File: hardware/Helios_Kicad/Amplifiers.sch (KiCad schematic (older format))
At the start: 31 parts, among them U6 TL084_v, U7 LM358, U8 TL084_v

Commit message: redone pcb, driver and firmware working-ish
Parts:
- removed R22, R23: 10k, Resistors_SMD:R_0603, symbol R
- added R16, R17, R24, R25, R30, R41, R42: 5.11k, Resistors_SMD:R_0603, symbol R
- added R18, R19: 10k, Resistors_SMD:R_0603, symbol R
- added R33, R34: 1.65k, Resistors_SMD:R_0603, symbol R
- renumbered C12 to C13, C13 to C14, C14 to C15, C15 to C16, C16 to C17, C17 to C18, R18 to R14, R19 to R15, R24 to R22, R25 to R23, R30 to R31, R31 to R32, R32 to R35, R33 to R36, R34 to R37, R35 to R38, R36 to R39, R37 to R40, R38 to R43, R39 to R44
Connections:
- net -B is gone; now on net +B: U6.7 (Out)
- net -R is gone; now on net +R: U6.14 (Out)
- net +B: now also R21.1; no longer R21.2
- net +G: now also R29.1, U6.8 (Out); no longer R26.2
- net +Intensity: now also R28.1, U6.1 (Out); no longer R27.2
- net +R: now also R20.1; no longer R20.2
- net GND: now also R20.2, R21.2, R26.1, R27.1, R28.2, R29.2, R18.1, R19.1, R41.2, R42.2; no longer U6.10 (+In), U6.12 (+In), U6.3 (+In), U6.5 (+In), U8.12 (+In), U8.5 (+In)
- net Offset: now also R33.2, R34.2; no longer U8.10 (+In), U8.3 (+In)
- net Shutter: now also R30.2; no longer U7.5 (+)
- net at U6.13 (-In): now also R18.2; no longer R20.1
- net at U6.6 (-In): now also R19.2; no longer R21.1
- removed net -G: R28.1, U6.8 (Out)
- removed net -Intensity: R29.1, U6.1 (Out)
- new net: R33.1, U8.3 (+In)
- new net: R42.1, U8.5 (+In)
- new net: R41.1, U8.12 (+In)
- new net: R34.1, U8.10 (+In)
- new net: R16.1, U6.12 (+In)
- new net: R24.1, U6.10 (+In)
- new net: R27.2, U6.9 (-In)
- new net: R17.1, U6.5 (+In)
- new net: R26.2, U6.2 (-In)
- new net: R25.1, U6.3 (+In)
- new net: R30.1, U7.5 (+)
- new net B: R17.2
- new net G: R24.2
- new net Intensity: R25.2
- new net R: R16.2
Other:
- moved on the sheet: U6A, U6B

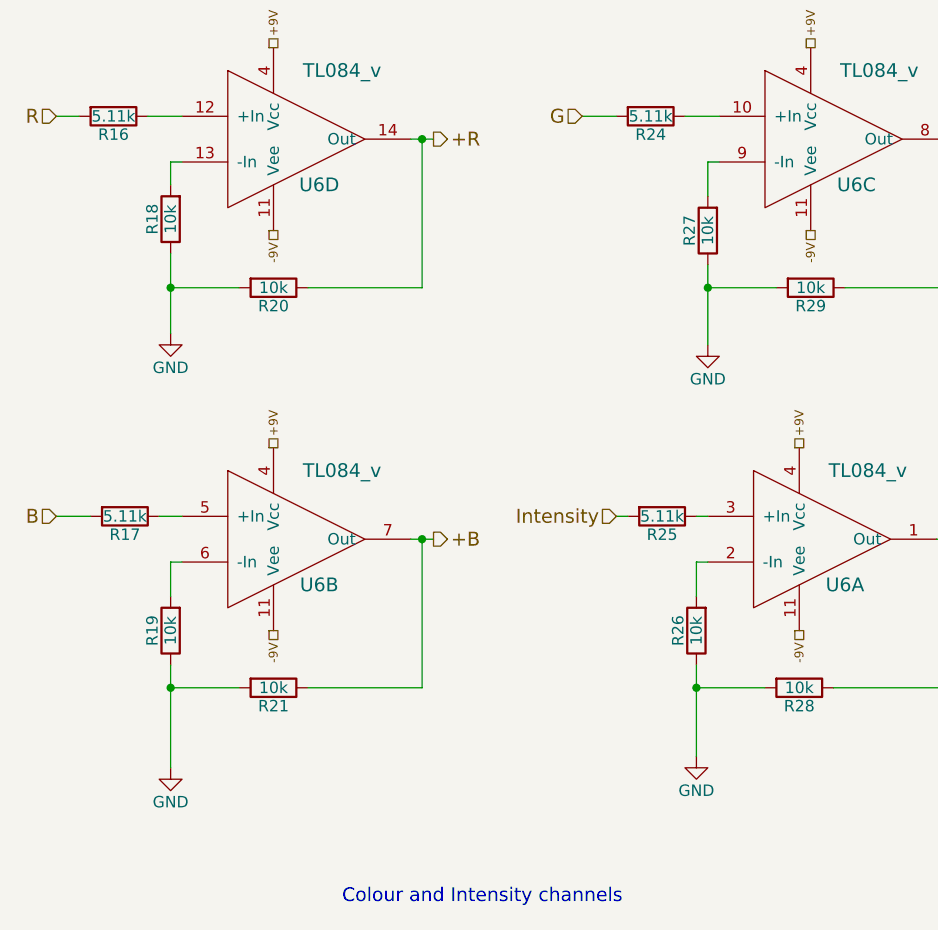
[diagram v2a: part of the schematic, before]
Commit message: fix color amps error
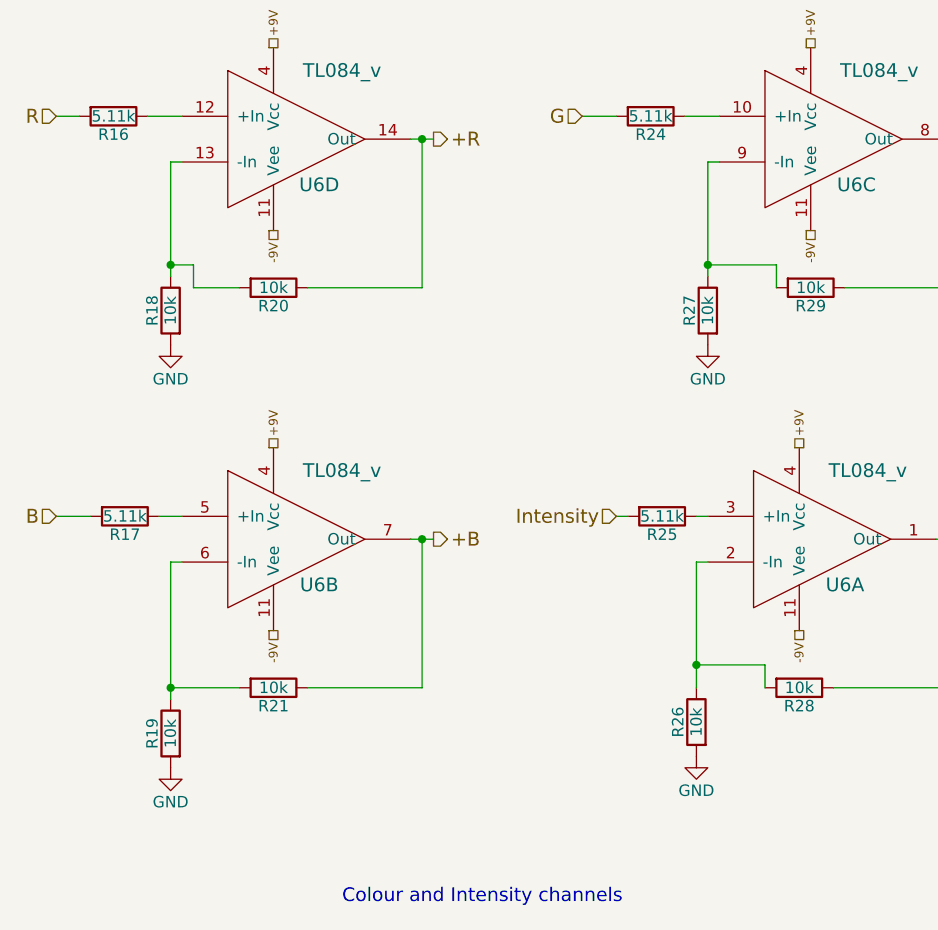
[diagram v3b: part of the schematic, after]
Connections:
- net GND: now also R18.2, R19.2, R26.2, R27.2; no longer R18.1, R19.1, R20.2, R21.2, R26.1, R27.1, R28.2, R29.2
- net at U6.13 (-In): now also R18.1, R20.2; no longer R18.2
- net at U6.9 (-In): now also R27.1, R29.2; no longer R27.2
- net at U6.6 (-In): now also R19.1, R21.2; no longer R19.2
- net at U6.2 (-In): now also R26.1, R28.2; no longer R26.2
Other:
- moved on the sheet: R18

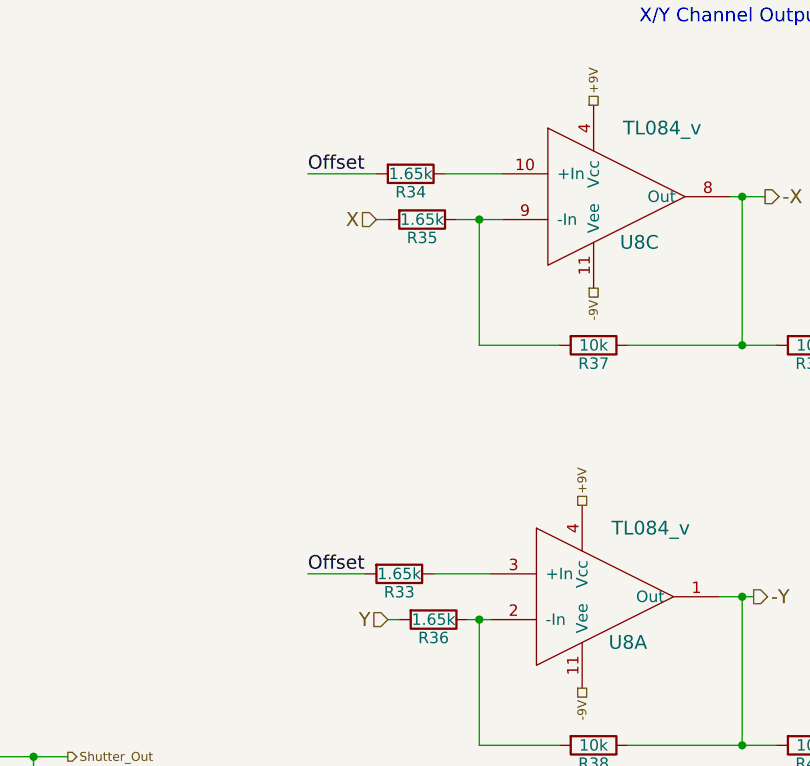
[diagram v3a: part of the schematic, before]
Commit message: removed uneccessary resistors
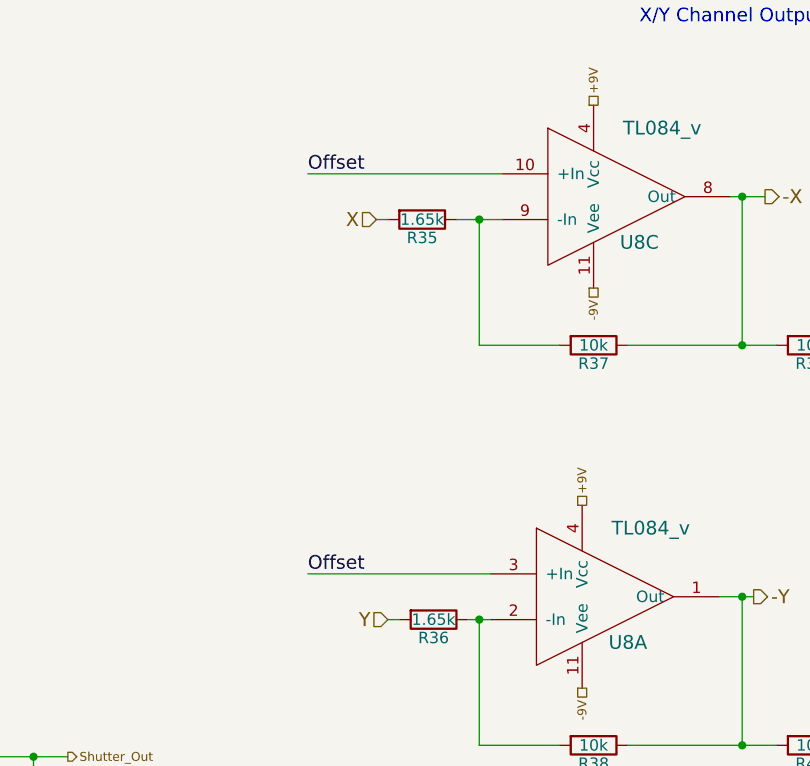
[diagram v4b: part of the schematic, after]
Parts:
- removed R33, R34: 1.65k, Resistors_SMD:R_0603, symbol R
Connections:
- net Offset: now also U8.10 (+In), U8.3 (+In)
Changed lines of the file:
@@
 	2800 6400 2800 6550
 Wire Wire Line
-	7650 3600 7900 3600
-Wire Wire Line
-	7600 5350 7850 5350
+	7050 3600 7900 3600
+Wire Wire Line
+	7050 5350 7850 5350
 Wire Wire Line
 	7350 3800 7400 3800
@@
 	9450 3600 9500 3600
 $Comp
-L R R33
-U 1 1 5792F098
-P 7450 5350
-F 0 "R33" V 7530 5350 50  0000 C CNN
-F 1 "1.65k" V 7450 5350 50  0000 C CNN
-F 2 "Resistors_SMD:R_0603" V 7380 5350 50  0001 C CNN
-F 3 "" H 7450 5350 50  0000 C CNN
-	1    7450 5350
-	0    1    1    0
-$EndComp
-Wire Wire Line
-	7050 5350 7300 5350
-$Comp
-L R R34
-U 1 1 5792F4A6
-P 7500 3600
-F 0 "R34" V 7580 3600 50  0000 C CNN
-F 1 "1.65k" V 7500 3600 50  0000 C CNN
-F 2 "Resistors_SMD:R_0603" V 7430 3600 50  0001 C CNN
-F 3 "" H 7500 3600 50  0000 C CNN
-	1    7500 3600
-	0    1    1    0
-$EndComp
-Wire Wire Line
-	7350 3600 7050 3600
-$Comp
 L R R30
